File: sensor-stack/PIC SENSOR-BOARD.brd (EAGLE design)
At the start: 40.4 x 75 mm, 27 parts

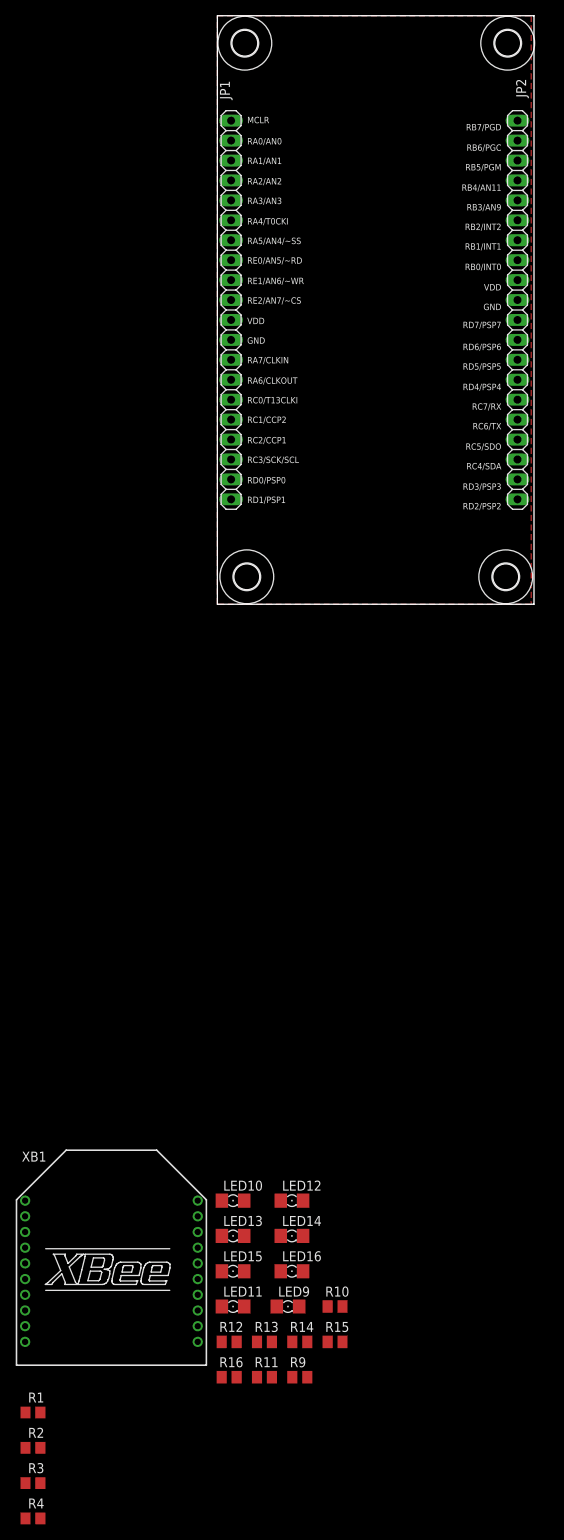
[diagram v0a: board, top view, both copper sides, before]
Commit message: Added Sensor Board
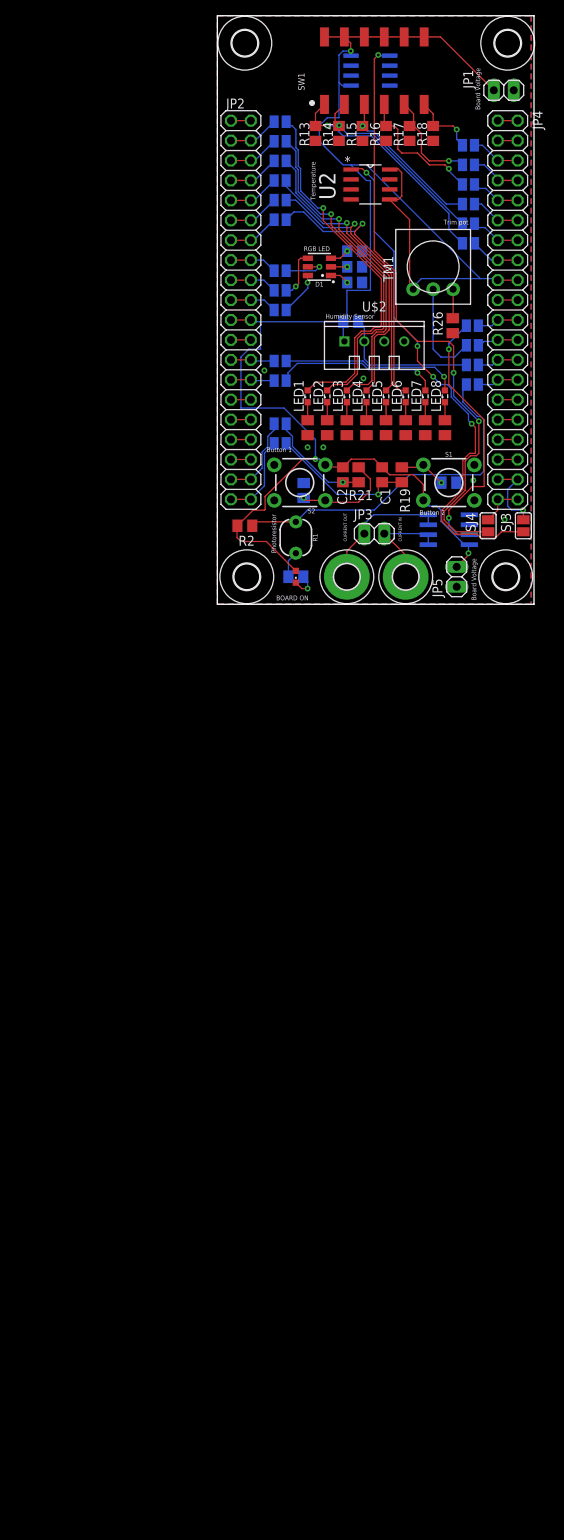
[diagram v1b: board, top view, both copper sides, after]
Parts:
- removed LED10, LED11, LED12, LED13, LED14, LED15, LED16: (no value), eagle-ltspice:LED_1206
- removed XB1: XBEE, maxstream:XBEE
- added C1, C2: (no value), rcl:C0805
- added D1: RGB, SparkFun-LED:PLCC-6-LED
- added H5, H6: MOUNT-PAD-ROUND3.3, holes:3,3-PAD
- added JP3, JP5: (no value), pinhead:1X02
- added JP4: (no value), adafruit:2X20
- added LED1, LED2, LED3, LED4, LED5, LED6, LED7, LED8: (no value), led:SML0603
- added R17, R18, R22, R23, R24: (no value), rcl:R0805
- added R19, R20, R21, R25, R26, R5, R6, R7, R8: (no value), rcl:M0805
- added S1, S2: MOMENTARY-SWITCH-SPST-PTH-6.0MM, SparkFun-Switches:TACTILE_SWITCH_PTH_6.0MM
- added SJ1, SJ10, SJ11, SJ12, SJ13, SJ14, SJ15, SJ16, SJ17, SJ18, SJ19, SJ2, SJ20, SJ21, SJ22, SJ23, SJ24, SJ25, SJ3, SJ4, SJ5, SJ6, SJ7, SJ8, SJ9: (no value), jumper:SJ
- added SW1: DIP-06, SparkFun-Switches:DIPSWITCH-06-SMD
- added TM1: (no value), adafruit:TRIM-3386
- added U$1: ACS723, SparkFun-Sensors:SO08
- added U$2: TEMP-HUM-SENSOR-DHT11, diy-modules:TEMP-HUM-SENSOR-DHT11
- added U1, U2: TMP36GSZ, ADI-Phase-2:SOIC127P600X175-8N
- JP1: device pinhead:1X20 -> pinhead:1X02
- JP2: device pinhead:1X20 -> adafruit:2X20
- LED9: device eagle-ltspice:LED_1206 -> led:CHIPLED_0603
- R1: value (none) -> PHOTOCELLPTH; device rcl:R0805 -> SparkFun-Sensors:PHOTOCELL
- R13, R14, R15, R16: device rcl:M0805 -> rcl:R0805
- R2, R4: device rcl:R0805 -> rcl:M0805
- R3: value (none) -> 5K; device rcl:R0805 -> rcl:M0805
- moved R16 159.8 mm to (21.5, 60.0), turned to 90 degrees
- moved R13 154.1 mm to (12.5, 60.0), turned to 90 degrees
- moved R14 154.1 mm to (15.5, 60.0), turned to 90 degrees
- moved R15 154.0 mm to (18.5, 60.0), turned to 90 degrees
- moved R3 153.4 mm to (17.0, 36.0), flipped to the bottom
- moved R4 142.2 mm to (29.5, 15.5), flipped to the bottom
- moved R11 122.7 mm to (26.5, 22.5), turned to 90 degrees
- moved R9 121.5 mm to (21.5, 22.5), turned to 90 degrees
- moved R2 120.6 mm to (3.50, 10.0), turned to 180 degrees
- moved R12 119.7 mm to (29.0, 22.5), turned to 90 degrees
- moved R1 116.4 mm to (10.0, 8.50), turned to 270 degrees
- moved R10 112.4 mm to (24.0, 22.5), turned to 90 degrees
- moved LED9 93.0 mm to (10.0, 3.50), turned to 180 degrees
- moved JP1 44.6 mm to (36.5, 65.5), turned to 180 degrees
- moved JP2 35.2 mm to (3.00, 37.5)
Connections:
- removed net N$10: LED10.A
- removed net N$11: LED11.A
- removed net N$12: LED12.A
- removed net N$13: LED13.A
- removed net N$14: LED14.A
- removed net N$15: LED15.A
- removed net N$16: LED16.A
- removed net N$17: LED9.C, R9.2
- removed net N$18: LED10.C, R10.2
- removed net N$19: LED11.C, R11.2
- removed net N$2: R3.2, R4.2, XB1.3
- removed net N$20: LED12.C, R12.2
- removed net N$21: LED13.C, R13.2
- removed net N$22: LED14.C, R14.2
- removed net N$23: LED15.C, R15.2
- removed net N$24: LED16.C, R16.2
- removed net N$3: R1.2, R2.2, XB1.2
- removed net N$9: LED9.A
- removed net RA0: JP1.2
- removed net RA1: JP1.3
- removed net RA2: JP1.4
- removed net RA3: JP1.5
- removed net RA4: JP1.6
- removed net RA5: JP1.7
- removed net RA6: JP1.14
- removed net RA7: JP1.13
- removed net RB0: JP2.8
- removed net RB1: JP2.7
- removed net RB2: JP2.6
- removed net RB3: JP2.5
- removed net RB4: JP2.4
- removed net RB5: JP2.3
- removed net RD0: JP1.19
- removed net RD1: JP1.20
- removed net RD2: JP2.20
- removed net RD3: JP2.19
- removed net RD4: JP2.14
- removed net RD5: JP2.13
- removed net RD6: JP2.12
- removed net RD7: JP2.11
- removed net RE0: JP1.8
- removed net RE1: JP1.9
- removed net RE2: JP1.10
- new net BLUE+: D1.AB, SJ16.1
- new net BLUE-: D1.CB, R24.1
- new net BLUE_ON: JP2.19, JP2.20, SJ16.2
- new net CAP2_NEG: C1.2, R19.1, SJ14.1
- new net CAP_NEG: C2.2, R21.1, SJ15.1
- new net CURRENT_LINE: SJ2.1, U$1.7
- new net CURRENT_OUT: JP4.21, JP4.22, SJ2.2
- new net DIP1_LINE: R13.2, SJ25.1, SW1.1
- new net DIP1_OUT: JP4.15, JP4.16, SJ25.2
- new net DIP2_LINE: R14.2, SJ24.1, SW1.2
- new net DIP2_OUT: JP4.13, JP4.14, SJ24.2
- new net DIP3_LINE: R15.2, SJ23.1, SW1.3
- new net DIP3_OUT: JP4.11, JP4.12, SJ23.2
- new net DIP4_LINE: R16.2, SJ22.1, SW1.4
- new net DIP4_OUT: JP4.10, JP4.9, SJ22.2
- new net DIP5_LINE: R17.2, SJ21.1, SW1.5
- new net DIP5_OUT: JP4.7, JP4.8, SJ21.2
- new net DIP6_LINE: R18.2, SJ20.1, SW1.6
- new net DIP6_OUT: JP4.5, JP4.6, SJ20.2
- new net GREEN+: D1.AG, SJ17.1
- new net GREEN-: D1.CG, R23.1
- new net GREEN_ON: JP2.17, JP2.18, SJ17.2
- new net HUM_DATA: R3.1, SJ5.2, U$2.2
- new net HUM_OUT: JP4.25, JP4.26, SJ5.1
- new net IP+: H5.B3,3, JP3.2, U$1.1, U$1.2
- new net IP-: H6.B3,3, JP3.1, U$1.3, U$1.4
- new net L1+: LED1.A, SJ6.1
- new net L1-: LED1.C, R5.2
- new net L2+: LED2.A, SJ7.1
- new net L2-: LED2.C, R6.2
- new net L3+: LED3.A, SJ8.1
- new net L3-: LED3.C, R7.2
- new net L4+: LED4.A, SJ9.1
- new net L4-: LED4.C, R8.2
- new net L5+: LED5.A, SJ10.1
- new net L5-: LED5.C, R9.2
- new net L6+: LED6.A, SJ11.1
- new net L6-: LED6.C, R10.2
- new net L7+: LED7.A, SJ12.1
- new net L7-: LED7.C, R11.2
- new net L8+: LED8.A, SJ13.1
- new net L8-: LED8.C, R12.2
- new net LED1_ON: JP2.3, JP2.4, SJ6.2
- new net LED2_ON: JP2.5, JP2.6, SJ7.2
- new net LED3_ON: JP2.7, JP2.8, SJ8.2
- new net LED4_ON: JP2.10, JP2.9, SJ9.2
- new net LED5_ON: JP2.11, JP2.12, SJ10.2
- new net LED6_ON: JP2.13, JP2.14, SJ11.2
- new net LED7_ON: JP2.27, JP2.28, SJ12.2
- new net LED8_ON: JP2.25, JP2.26, SJ13.2
- new net LIGHT_LINE: R1.1, R2.1, SJ1.1
- new net LIGHT_OUT: JP4.27, JP4.28, SJ1.2
- new net POWER-: LED9.C, R25.1
- new net RED+: D1.AR, SJ18.1
- new net RED-: D1.CR, R22.1
- new net RED_ON: JP2.15, JP2.16, SJ18.2
- new net SWITCH1_OUT: JP2.37, JP2.38, SJ15.2
- new net SWITCH2_OUT: JP2.39, JP2.40, SJ14.2
- new net SW_NEG: R20.2, R21.2, S2.1
- new net SW_NEG2: R19.2, R4.2, S1.1
- new net T1_LINE: SJ4.1, U1.1
- new net T2_LINE: SJ3.1, U2.1
- new net TEMP1_OUT: JP4.39, JP4.40, SJ4.2
- new net TEMP2_OUT: JP4.37, JP4.38, SJ3.2
- new net TRIM: R26.2, TM1.3
- new net TRIM_JUMP: SJ19.2, TM1.2
- new net TRIM_OUT: JP4.23, JP4.24, SJ19.1
- net GND: now also JP1.1, JP2.23, JP2.24, JP4.19, JP4.20, JP5.1, R1.2, R17.1, R18.1, R20.1, R22.2, R23.2, R24.2, R25.2, R26.1, R4.1, R5.1, R6.1, R7.1, R8.1, U$1.5, U$1.6, U$2.4, U1.4, U2.4; no longer JP1.12, JP2.10, XB1.10
- net MCLR: now also JP2.1, JP2.2; no longer JP1.1
- net RB6/PGC: now also JP4.3, JP4.4; no longer JP2.2
- net RB7/PGD: now also JP4.1, JP4.2; no longer JP2.1
- net RC0: now also JP2.29, JP2.30; no longer JP1.15
- net RC1: now also JP2.31, JP2.32; no longer JP1.16
- net RC2: now also JP2.33, JP2.34; no longer JP1.17
- net RC3: now also JP2.35, JP2.36; no longer JP1.18
- net RC4: now also JP4.35, JP4.36; no longer JP2.18
- net RC5: now also JP4.33, JP4.34; no longer JP2.17
- net RC6: now also JP4.31, JP4.32; no longer JP2.16
- net RC7: now also JP4.29, JP4.30; no longer JP2.15
- net VDD: now also C1.1, C2.1, JP1.2, JP2.21, JP2.22, JP4.17, JP4.18, JP5.2, LED9.A, R2.2, R3.2, S1.3, S2.3, SW1.10, SW1.11, SW1.12, SW1.7, SW1.8, SW1.9, TM1.1, U$1.8, U$2.1, U1.5, U1.8, U2.5, U2.8; no longer JP1.11, JP2.9, XB1.1
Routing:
- net VDD: track 1.36 -> 228.6 mm, vias 0 -> 3
- net T1_LINE: track 0.00 -> 77.3 mm, vias 0 -> 3
- net T2_LINE: track 0.00 -> 66.7 mm, vias 0 -> 4
- net L1+: track 0.00 -> 47.0 mm, vias 0 -> 1
- net LIGHT_LINE: track 0.00 -> 45.0 mm
- net L2+: track 0.00 -> 42.9 mm, vias 0 -> 1
- net L3+: track 0.00 -> 39.5 mm, vias 0 -> 1
- net L6+: track 0.00 -> 36.4 mm, vias 0 -> 1
- net L4+: track 0.00 -> 35.8 mm, vias 0 -> 1
- net L5+: track 0.00 -> 34.3 mm, vias 0 -> 1
- net CURRENT_LINE: track 0.00 -> 34.1 mm, vias 0 -> 2
- net DIP1_LINE: track 0.00 -> 29.4 mm, vias 0 -> 1
- net DIP2_LINE: track 0.00 -> 24.7 mm, vias 0 -> 1
- net L8+: track 0.00 -> 22.8 mm, vias 0 -> 1
- net L7+: track 0.00 -> 21.3 mm, vias 0 -> 1
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- added copper zone on layer 16, net GND
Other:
- board text added: "BOARD ON"
- board text added: "Board Voltage"
- board text added: "Button 1"
- board text added: "Button 2"
- board text added: "CURRENT IN"
- board text added: "CURRENT OUT"
- board text added: "Current Sensor"
- board text added: "Humidity Sensor"
- board text added: "PIC18 Sensor & Peripheal Board EE 310 Created By David Story Meadowview Lab"
- board text added: "Photoresistor"
- board text added: "RGB LED"
- board text added: "Temperature"
- board text added: "Trim pot"
- board text removed: "GND"
- board text removed: "MCLR"
- board text removed: "PIC18 Sensor Board Created By David Story Meadowview Labs"
- board text removed: "RA0/AN0"
- board text removed: "RA1/AN1"
- board text removed: "RA2/AN2"
- board text removed: "RA3/AN3"
- board text removed: "RA4/T0CKI"
- board text removed: "RA5/AN4/~SS"
- board text removed: "RA6/CLKOUT"
- board text removed: "RA7/CLKIN"
- board text removed: "RB0/INT0"
- board text removed: "RB1/INT1"
- board text removed: "RB2/INT2"
- board text removed: "RB3/AN9"
- board text removed: "RB4/AN11"
- board text removed: "RB5/PGM"
- board text removed: "RB6/PGC"
- board text removed: "RB7/PGD"
- board text removed: "RC0/T13CLKI"
- board text removed: "RC1/CCP2"
- board text removed: "RC2/CCP1"
- board text removed: "RC3/SCK/SCL"
- board text removed: "RC4/SDA"
- board text removed: "RC5/SDO"
- board text removed: "RC6/TX"
- board text removed: "RC7/RX"
- board text removed: "RD0/PSP0"
- board text removed: "RD1/PSP1"
- board text removed: "RD2/PSP2"
- board text removed: "RD3/PSP3"
- board text removed: "RD4/PSP4"
- board text removed: "RD5/PSP5"
- board text removed: "RD6/PSP6"
- board text removed: "RD7/PSP7"
- board text removed: "RE0/AN5/~RD"
- board text removed: "RE1/AN6/~WR"
- board text removed: "RE2/AN7/~CS"
- board text removed: "VDD"
